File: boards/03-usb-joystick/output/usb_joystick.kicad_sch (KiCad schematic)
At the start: 12 parts, among them J1 USB-C, J2 Joystick, SW1 Button, SW2 Button, SW3 Button, SW4 Button, U1 MCU, Y1 16MHz

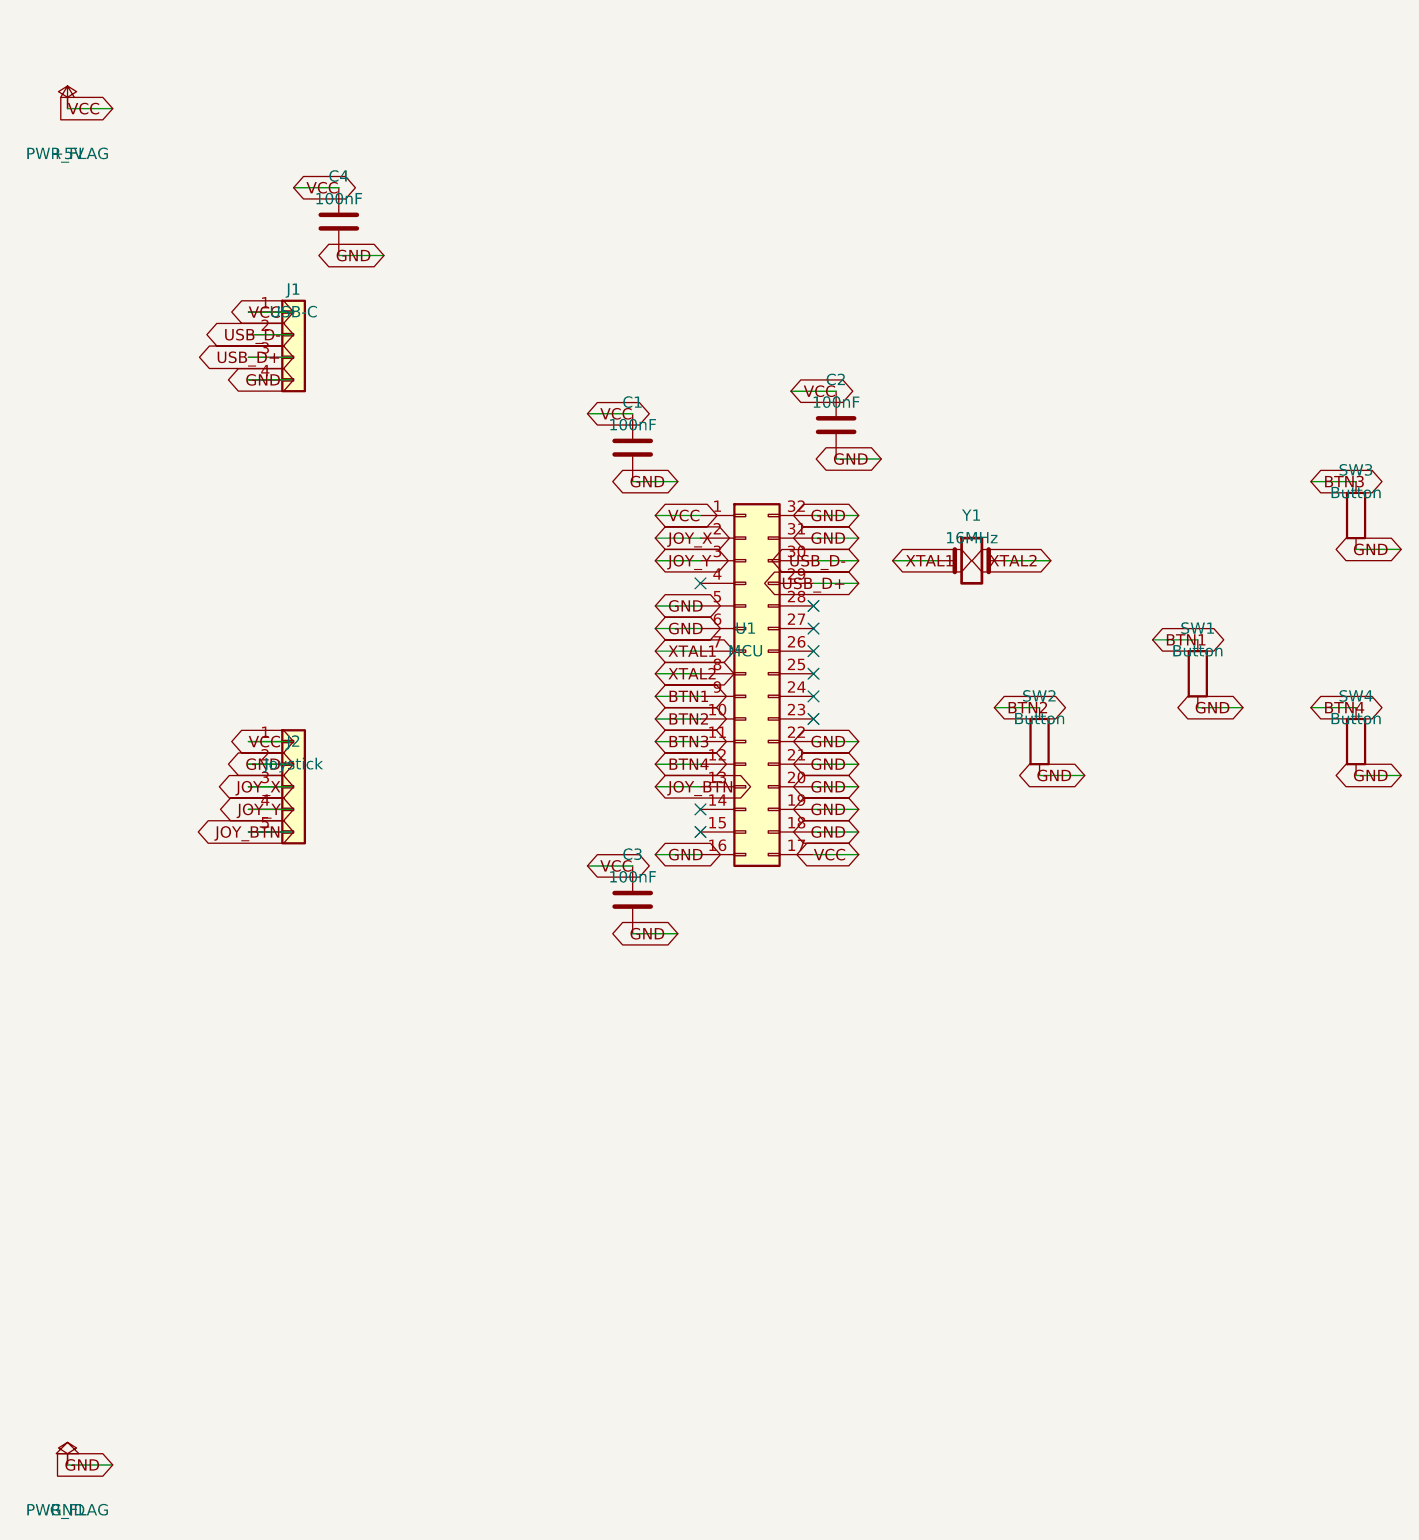
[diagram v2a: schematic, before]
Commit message: fix(boards/03): close reach gap to 13/13 + 0 DRC at jlcpcb-tier1 (closes #3410)
Board 03's production routing topped out at 77% (audit #3402) because the
committed board and its toolchain had FIVE stacked defects:

1. Generator drift: generate_design.py carried its own stale 60x40mm PCB
   copy (pre-#2527 pin map) that main() wrote over the canonical
   generate_pcb.py 80x60mm layout. The audit measured the stale board.
   The PCB step now delegates to generate_pcb.py (mirrors #3308).
2. J1 USB-C re-spin: the demo footprint mirrored the receptacle tongue,
   placing USB_D+/USB_D- tails in an X-crossover whose tie stubs
   physically overlapped (the allowlisted "structural" intra-pair
   violation). Same-signal tails now exit in the same column - the exit
   clause the DRC allowlist named since #3183.
3. MST tie-group representative: reduce_pads_after_intra_ic picked the
   FIRST pad of an intra-IC group, handing A* a start pad boxed in by the
   USB-C escape belt. It now picks the member closest to the net's
   external centroid (BLOCKED_BY_COMPONENT on an empty board, fixed).
4. Escape via-fanout: _escape_usb_c_connector built an alternating-layer
   via fanout inside J1 (sub-pitch via spacing = the dominant DRC error
   cluster). Column-aligned connectors now defer entirely to the main
   router; legacy mirrored footprints (board 06) keep #2919 behavior.
5. auto-pour zone deletion: _detect_uninset_zones subtracted board_origin
   from already-board-relative Zone.polygon vertices, flagging every
   hand-tuned zone as un-inset and silently replacing the GND/VCC/VBUS
   pour set with conflicting auto zones (stranding 30/33 GND pads).

Plus: generate_pcb.py now emits the full GND(F+B)/VCC/VBUS pour set and
a KiCad-10 header (kicad-cli rejects 20240108-with-zones, which silently
broke zone fill/DRC/gerber export), the modern (locked yes) form (with
schema-side parsing so anchor logic still sees locks), filter rows moved
off Steiner-junction lines, and C4 out of the D+/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
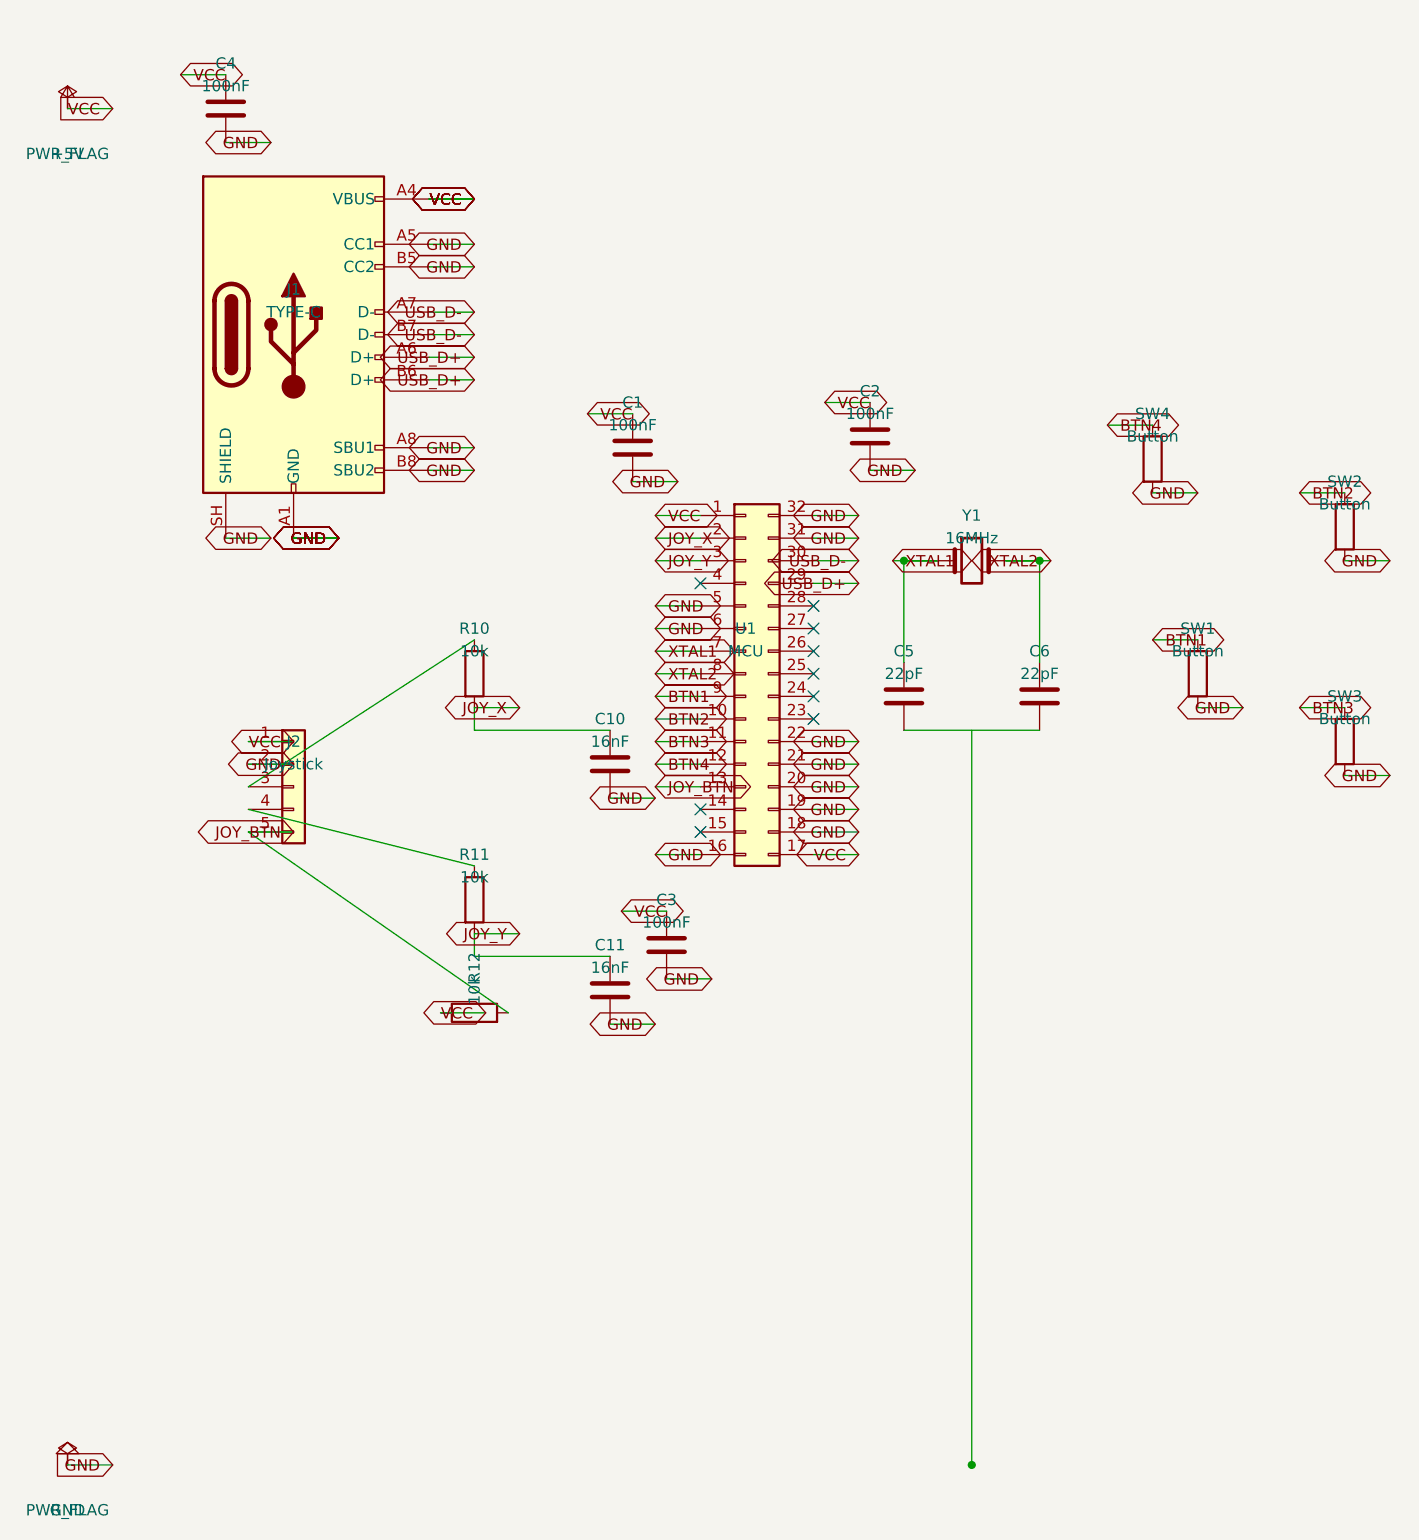
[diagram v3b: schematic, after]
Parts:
- removed J1: USB-C, symbol Connector_Generic:Conn_01x04
- added C10, C11: 16nF, Capacitor_SMD:C_0402_1005Metric, symbol Device:C
- added C5, C6: 22pF, Capacitor_SMD:C_0402_1005Metric, symbol Device:C
- added J1: TYPE-C, Connector_USB:USB_C_Receptacle_GCT_USB4105, symbol Connector:USB_C_Receptacle_USB2.0_16P
- added R10, R11, R12: 10k, Resistor_SMD:R_0402_1005Metric, symbol Device:R
- C1, C2, C3, C4: footprint (none) -> Capacitor_SMD:C_0402_1005Metric
- J2: footprint (none) -> Module:Joystick_Analog
- SW1, SW2, SW3, SW4: footprint (none) -> Button_Switch_SMD:SW_SPST_TL3342
- U1: footprint (none) -> Package_QFP:TQFP-32_7x7mm_P0.8mm
- Y1: footprint (none) -> Crystal:Crystal_HC49-U_Vertical
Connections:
- net +5V: now also J1.A4 (VBUS), J1.A9 (VBUS), J1.B4 (VBUS), J1.B9 (VBUS), R12.1
- net GND: now also C10.2, C11.2, J1.A1 (GND), J1.A12 (GND), J1.A5 (CC1), J1.A8 (SBU1), J1.B1 (GND), J1.B12 (GND), J1.B5 (CC2), J1.B8 (SBU2), J1.SH (SHIELD)
- net JOY_BTN: now also R12.2
- net JOY_X: now also C10.1, R10.2; no longer J2.3 (Pin_3)
- net JOY_Y: now also C11.1, R11.2; no longer J2.4 (Pin_4)
- net USB_D+: now also J1.A6 (D+), J1.B6 (D+)
- net USB_D-: now also J1.A7 (D-), J1.B7 (D-)
- net XTAL1: now also C5.1
- net XTAL2: now also C6.1
- new net: J2.3 (Pin_3), R10.1
- new net: J2.4 (Pin_4), R11.1
- new net: C5.2, C6.2

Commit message: fix(boards/03): reconcile schematic↔PCB net drift to one 16-net model (#3771)
Board-03 carried three diverging net models: generate_schematic.py,
generate_pcb.py, and a simplified inline schematic inside
generate_design.py:main(). compare_netlists reported 42 per-(ref,pad)
mismatches and fleet ship-ready flagged a schematic-drift blocker
(14 sch nets vs 16 PCB nets; +5V leak, USB_CC1/CC2/VBUS folded away).

Make the PCB's 16-net model the single source of truth and align the
schematic to it pad-for-pad:

- generate_design.py: delegate create_usb_joystick_schematic to
  generate_schematic.py (mirroring the PCB step's delegation), removing
  the third divergent inline schematic. Persist erc_report.json and
  write drc_report.json (--drc-only) so the fleet DRC/ERC legs are
  captured artifacts instead of n/a.
- generate_schematic.py: MCU pinout now matches the PCB pin_nets
  exactly (pins 2,3,9-15,23-32); USB connector exposes distinct VBUS /
  USB_CC1 / USB_CC2 (SBU -> NC, shield -> GND); power:+5V -> power:VCC;
  joystick filter R10/C10/R11/C11/R12 emitted explicitly to mirror the
  PCB's net topology; crystal load-cap ground bus labeled GND; C4 ties
  VBUS instead of VCC.
- generate_pcb.py: J2 pin order -> 1=VCC, 2=GND (standard
  Module:Joystick_Analog); J1 shield tabs named "SH" to match the
  schematic symbol; VCC pour extended west to cover the relocated J2.1.

Result: compare_netlists clean (0 mismatches), schematic_net_count ==
pcb_net_count == 16, 85/85 pads connected, DRC 0 blocking errors, fleet
ship-ready passed=true with no drift blocker. Adds a board-03 regression
test pinning clean LVS + matched 16-net sets.

Closes #3764

Co-authored-by: Claude Opus 4.8 <noreply@anthropic.com>
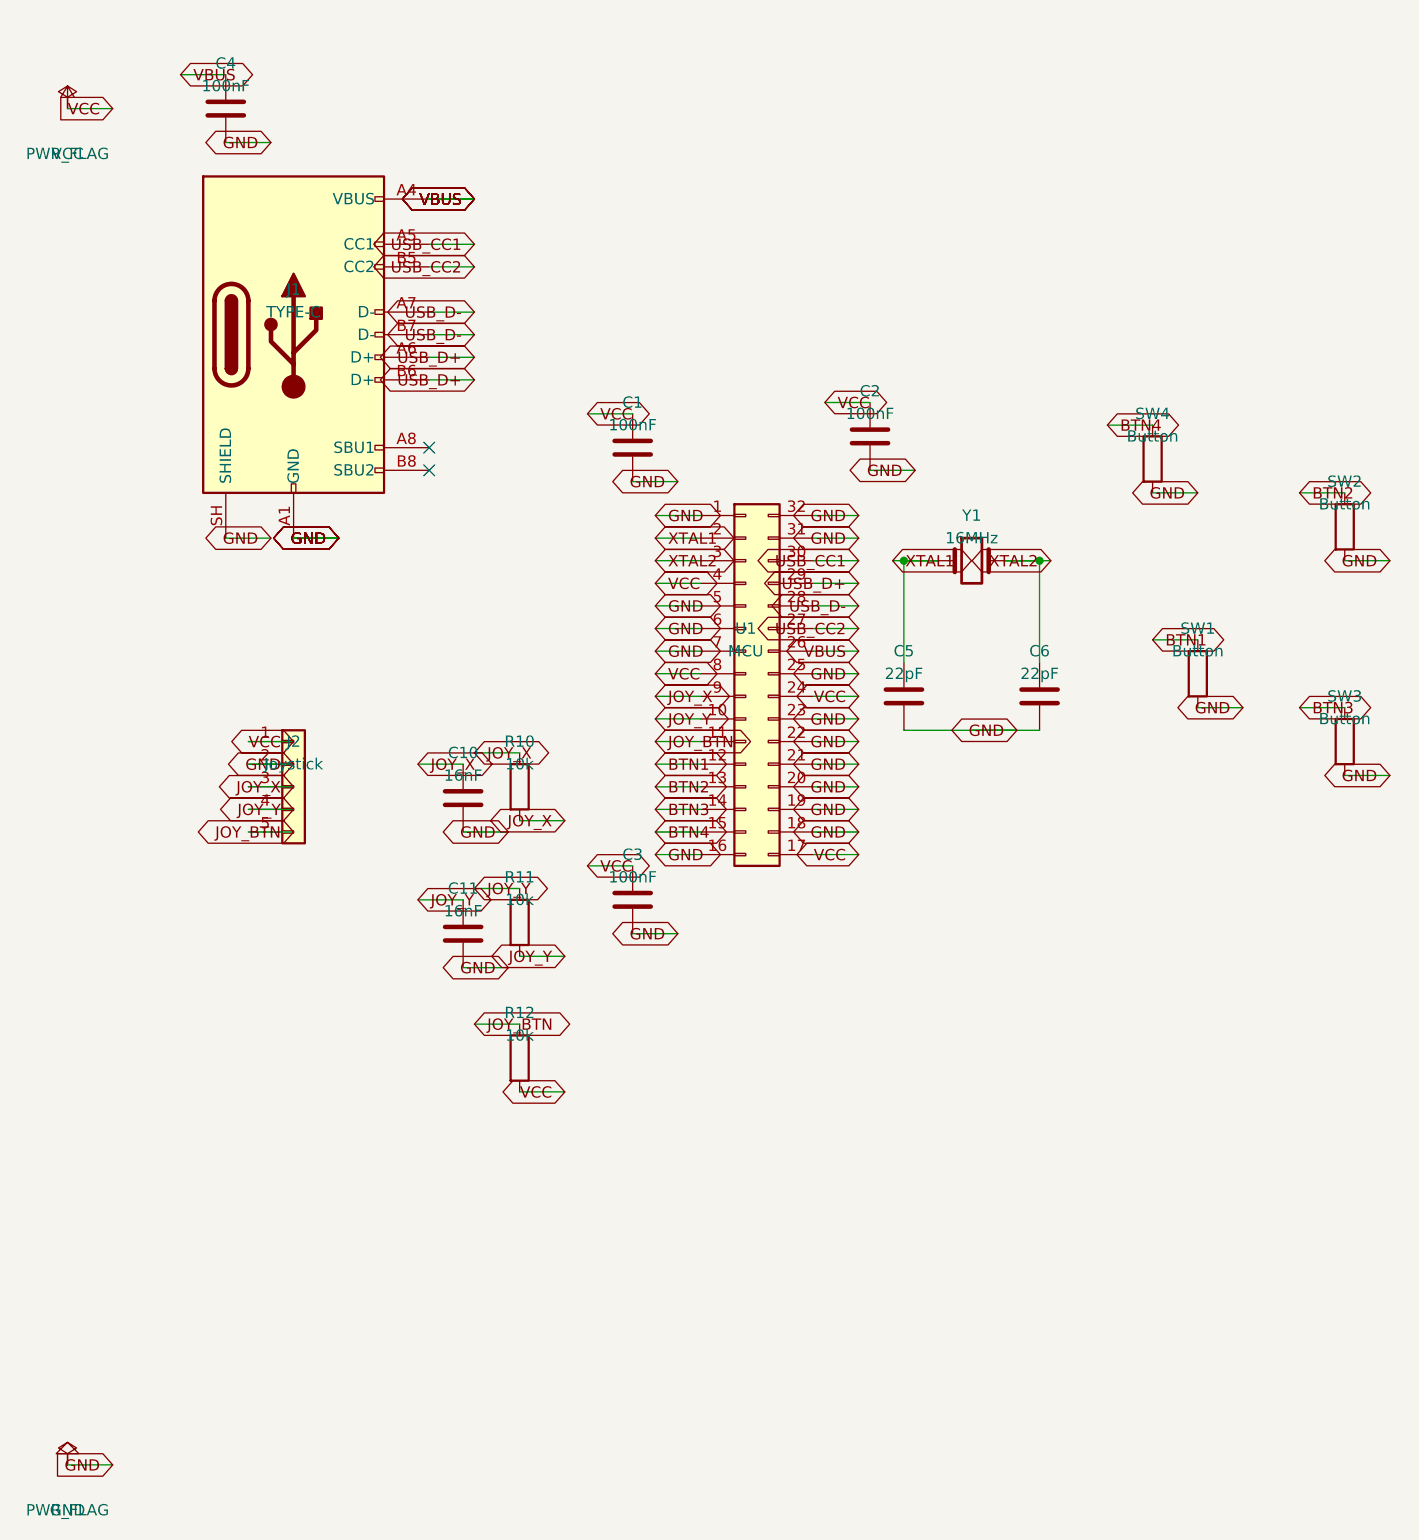
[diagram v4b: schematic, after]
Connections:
- net BTN1: now also U1.12 (Pin_12); no longer U1.9 (Pin_9)
- net BTN2: now also U1.13 (Pin_13); no longer U1.10 (Pin_10)
- net BTN3: now also U1.14 (Pin_14); no longer U1.11 (Pin_11)
- net BTN4: now also U1.15 (Pin_15); no longer U1.12 (Pin_12)
- net GND: now also C5.2, C6.2, U1.1 (Pin_1), U1.23 (Pin_23), U1.25 (Pin_25), U1.7 (Pin_7); no longer J1.A5 (CC1), J1.A8 (SBU1), J1.B5 (CC2), J1.B8 (SBU2)
- net JOY_BTN: now also R12.1, U1.11 (Pin_11); no longer R12.2, U1.13 (Pin_13)
- net JOY_X: now also J2.3 (Pin_3), R10.1, U1.9 (Pin_9); no longer U1.2 (Pin_2)
- net JOY_Y: now also J2.4 (Pin_4), R11.1, U1.10 (Pin_10); no longer U1.3 (Pin_3)
- net USB_D-: now also U1.28 (Pin_28); no longer U1.30 (Pin_30)
- net XTAL1: now also U1.2 (Pin_2); no longer U1.7 (Pin_7)
- net XTAL2: now also U1.3 (Pin_3); no longer U1.8 (Pin_8)
- net VCC: now reaches U1.24 (Pin_24)
- net VCC: now also C1.1, C2.1, C3.1, J2.1 (Pin_1), R12.2, U1.17 (Pin_17), U1.4 (Pin_4), U1.8 (Pin_8)
- net VBUS: now reaches U1.26 (Pin_26)
- net VBUS: now also C4.1, J1.A4 (VBUS), J1.A9 (VBUS), J1.B4 (VBUS), J1.B9 (VBUS)
- net USB_CC2: now reaches U1.27 (Pin_27)
- net USB_CC2: now also J1.B5 (CC2)
- removed net +5V: C1.1, C2.1, C3.1, C4.1, J1.A4 (VBUS), J1.A9 (VBUS), J1.B4 (VBUS), J1.B9 (VBUS), J2.1 (Pin_1), R12.1, U1.1 (Pin_1), U1.17 (Pin_17)
- new net USB_CC1: J1.A5 (CC1), U1.30 (Pin_30)
- no-connect marks 9 -> 2
